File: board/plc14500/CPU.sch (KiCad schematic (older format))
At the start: 67 parts, among them U3 74HC14, U6 NE555, U7 74HC590A, U8 LH5168, U9 MC14500

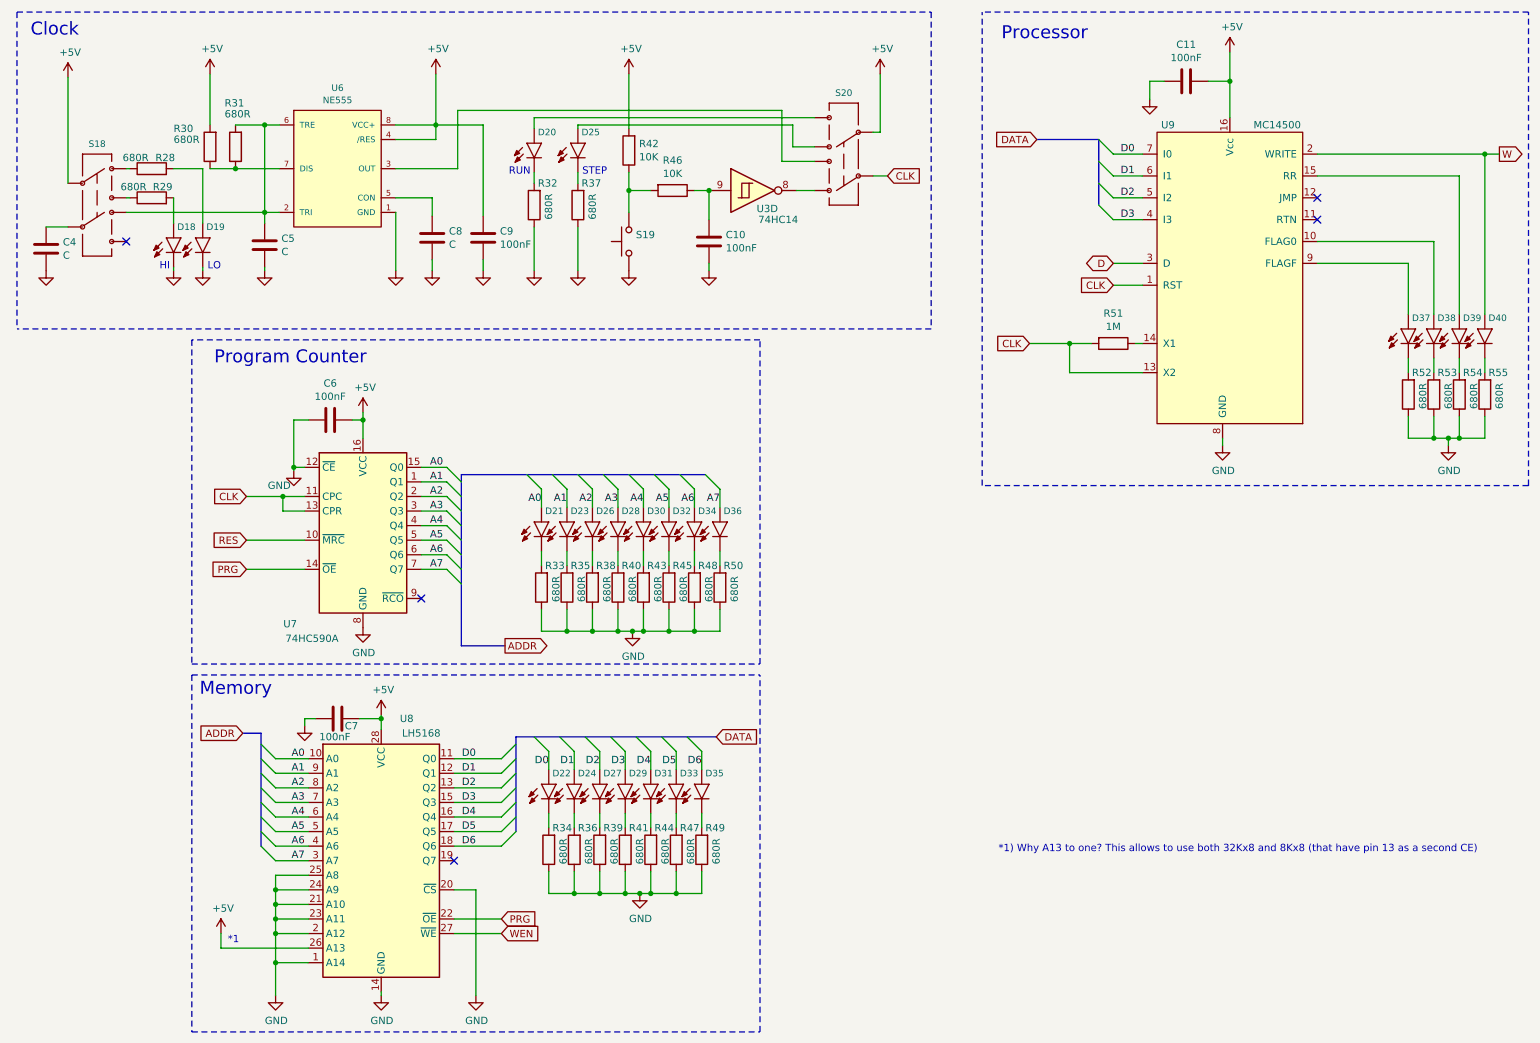
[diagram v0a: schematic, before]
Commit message: Schema updates, add loopback and timer
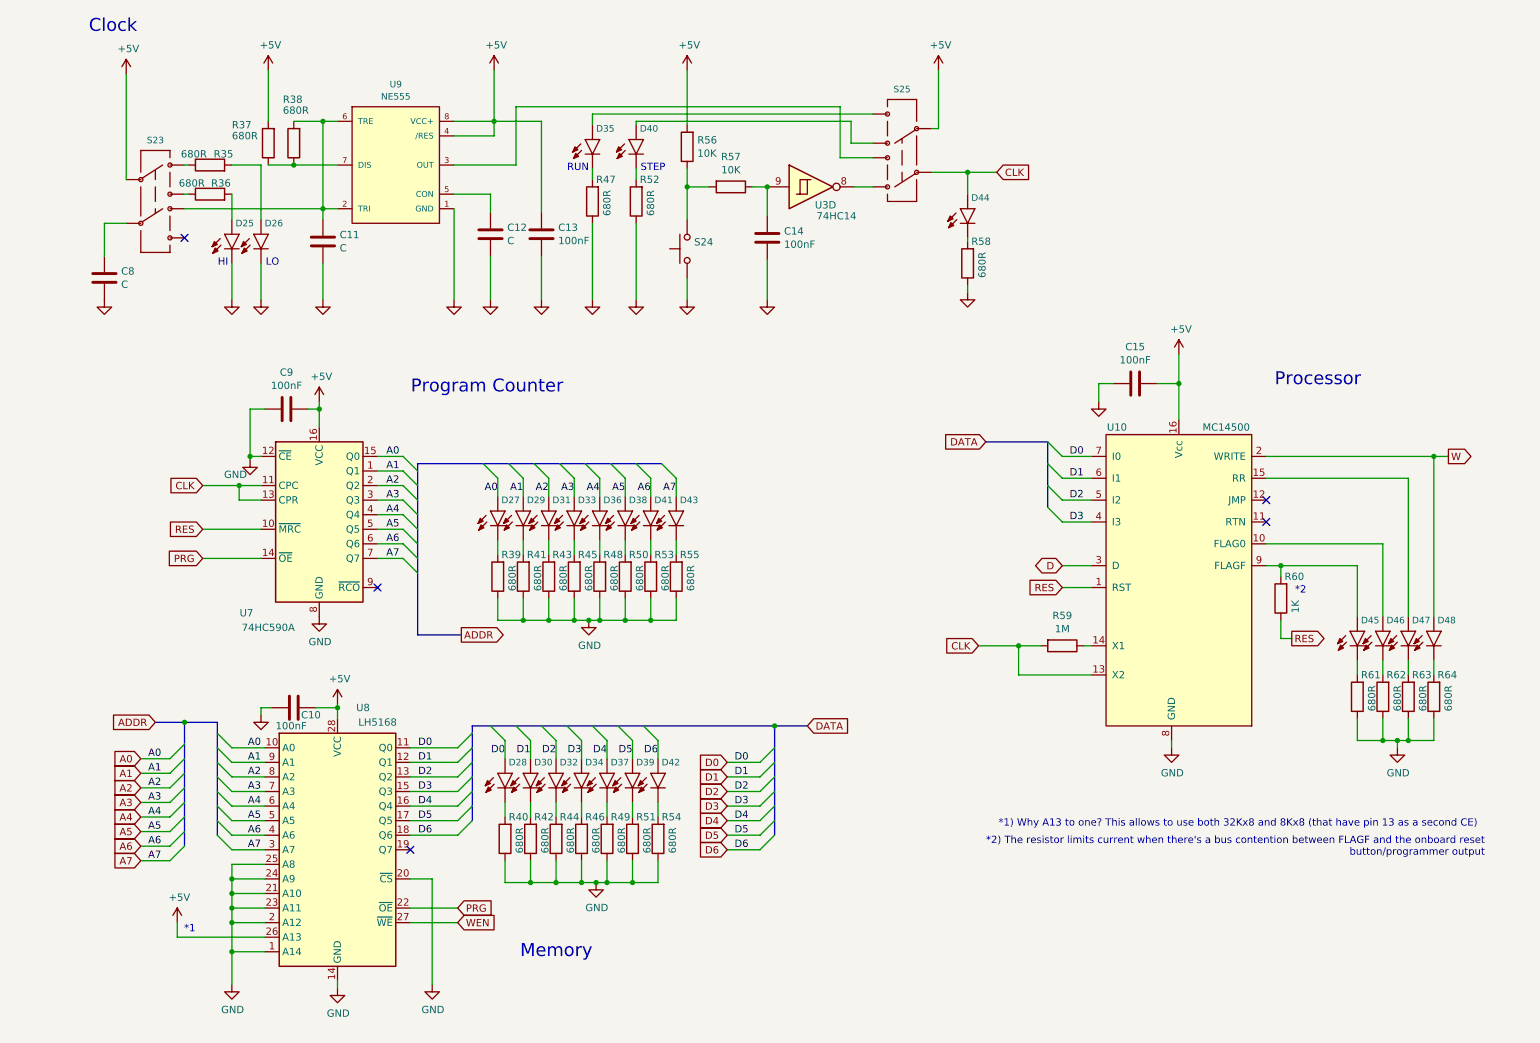
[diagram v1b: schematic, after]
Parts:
- added D44: LED5MM, plc14500:LED_5MM, symbol SparkFun-LED:LED5MM
- added R58: 680R, Resistor_THT:R_Axial_DIN0309_L9.0mm_D3.2mm_P12.70mm_Horizontal, symbol Device:R
- added R60: 1K, Resistor_THT:R_Axial_DIN0309_L9.0mm_D3.2mm_P12.70mm_Horizontal, symbol Device:R
- C10: renamed from C7; footprint (none) -> Capacitor_THT:C_Rect_L7.2mm_W2.5mm_P5.00mm_FKS2_FKP2_MKS2_MKP2
- C11: renamed from C5; footprint (none) -> Capacitor_THT:C_Rect_L7.2mm_W2.5mm_P5.00mm_FKS2_FKP2_MKS2_MKP2
- C12: renamed from C8; footprint (none) -> Capacitor_THT:C_Rect_L7.2mm_W2.5mm_P5.00mm_FKS2_FKP2_MKS2_MKP2
- C13: renamed from C9; footprint (none) -> Capacitor_THT:C_Rect_L7.2mm_W2.5mm_P5.00mm_FKS2_FKP2_MKS2_MKP2
- C14: renamed from C10; footprint (none) -> Capacitor_THT:C_Rect_L7.2mm_W2.5mm_P5.00mm_FKS2_FKP2_MKS2_MKP2
- C15: renamed from C11; footprint (none) -> Capacitor_THT:C_Rect_L7.2mm_W2.5mm_P5.00mm_FKS2_FKP2_MKS2_MKP2
- C8: renamed from C4; footprint (none) -> Capacitor_THT:C_Rect_L7.2mm_W2.5mm_P5.00mm_FKS2_FKP2_MKS2_MKP2
- C9: renamed from C6; footprint (none) -> Capacitor_THT:C_Rect_L7.2mm_W2.5mm_P5.00mm_FKS2_FKP2_MKS2_MKP2
- D25: renamed from D18; footprint LED_5MM -> plc14500:LED_5MM
- D26: renamed from D19; footprint LED_5MM -> plc14500:LED_5MM
- D27: renamed from D21; footprint LED_5MM -> plc14500:LED_5MM
- D28: renamed from D22; footprint LED_5MM -> plc14500:LED_5MM
- D29: renamed from D23; footprint LED_5MM -> plc14500:LED_5MM
- D30: renamed from D24; footprint LED_5MM -> plc14500:LED_5MM
- D31: renamed from D26; footprint LED_5MM -> plc14500:LED_5MM
- D32: renamed from D27; footprint LED_5MM -> plc14500:LED_5MM
- D33: renamed from D28; footprint LED_5MM -> plc14500:LED_5MM
- D34: renamed from D29; footprint LED_5MM -> plc14500:LED_5MM
- D35: renamed from D20; footprint LED_5MM -> plc14500:LED_5MM
- D36: renamed from D30; footprint LED_5MM -> plc14500:LED_5MM
- D37: renamed from D31; footprint LED_5MM -> plc14500:LED_5MM
- D38: renamed from D32; footprint LED_5MM -> plc14500:LED_5MM
- D39: renamed from D33; footprint LED_5MM -> plc14500:LED_5MM
- D40: renamed from D25; footprint LED_5MM -> plc14500:LED_5MM
- D41: renamed from D34; footprint LED_5MM -> plc14500:LED_5MM
- D42: renamed from D35; footprint LED_5MM -> plc14500:LED_5MM
- D43: renamed from D36; footprint LED_5MM -> plc14500:LED_5MM
- D45: renamed from D37; footprint LED_5MM -> plc14500:LED_5MM
- D46: renamed from D38; footprint LED_5MM -> plc14500:LED_5MM
- D47: renamed from D39; footprint LED_5MM -> plc14500:LED_5MM
- D48: renamed from D40; footprint LED_5MM -> plc14500:LED_5MM
- R35: renamed from R28; footprint (none) -> Resistor_THT:R_Axial_DIN0309_L9.0mm_D3.2mm_P12.70mm_Horizontal
- R36: renamed from R29; footprint (none) -> Resistor_THT:R_Axial_DIN0309_L9.0mm_D3.2mm_P12.70mm_Horizontal
- R37: renamed from R30; footprint (none) -> Resistor_THT:R_Axial_DIN0309_L9.0mm_D3.2mm_P12.70mm_Horizontal
- R38: renamed from R31; footprint (none) -> Resistor_THT:R_Axial_DIN0309_L9.0mm_D3.2mm_P12.70mm_Horizontal
- R39: renamed from R33; footprint (none) -> Resistor_THT:R_Axial_DIN0309_L9.0mm_D3.2mm_P12.70mm_Horizontal
- R40: renamed from R34; footprint (none) -> Resistor_THT:R_Axial_DIN0309_L9.0mm_D3.2mm_P12.70mm_Horizontal
- R41: renamed from R35; footprint (none) -> Resistor_THT:R_Axial_DIN0309_L9.0mm_D3.2mm_P12.70mm_Horizontal
- R42: renamed from R36; footprint (none) -> Resistor_THT:R_Axial_DIN0309_L9.0mm_D3.2mm_P12.70mm_Horizontal
- R43: renamed from R38; footprint (none) -> Resistor_THT:R_Axial_DIN0309_L9.0mm_D3.2mm_P12.70mm_Horizontal
- R44: renamed from R39; footprint (none) -> Resistor_THT:R_Axial_DIN0309_L9.0mm_D3.2mm_P12.70mm_Horizontal
- R45: renamed from R40; footprint (none) -> Resistor_THT:R_Axial_DIN0309_L9.0mm_D3.2mm_P12.70mm_Horizontal
- R46: renamed from R41; footprint (none) -> Resistor_THT:R_Axial_DIN0309_L9.0mm_D3.2mm_P12.70mm_Horizontal
- R47: renamed from R32; footprint (none) -> Resistor_THT:R_Axial_DIN0309_L9.0mm_D3.2mm_P12.70mm_Horizontal
- R48: renamed from R43; footprint (none) -> Resistor_THT:R_Axial_DIN0309_L9.0mm_D3.2mm_P12.70mm_Horizontal
- R49: renamed from R44; footprint (none) -> Resistor_THT:R_Axial_DIN0309_L9.0mm_D3.2mm_P12.70mm_Horizontal
- R50: renamed from R45; footprint (none) -> Resistor_THT:R_Axial_DIN0309_L9.0mm_D3.2mm_P12.70mm_Horizontal
- R51: renamed from R47; footprint (none) -> Resistor_THT:R_Axial_DIN0309_L9.0mm_D3.2mm_P12.70mm_Horizontal
- R52: renamed from R37; footprint (none) -> Resistor_THT:R_Axial_DIN0309_L9.0mm_D3.2mm_P12.70mm_Horizontal
- R53: renamed from R48; footprint (none) -> Resistor_THT:R_Axial_DIN0309_L9.0mm_D3.2mm_P12.70mm_Horizontal
- R54: renamed from R49; footprint (none) -> Resistor_THT:R_Axial_DIN0309_L9.0mm_D3.2mm_P12.70mm_Horizontal
- R55: renamed from R50; footprint (none) -> Resistor_THT:R_Axial_DIN0309_L9.0mm_D3.2mm_P12.70mm_Horizontal
- R56: renamed from R42; footprint (none) -> Resistor_THT:R_Axial_DIN0309_L9.0mm_D3.2mm_P12.70mm_Horizontal
- R57: renamed from R46; footprint (none) -> Resistor_THT:R_Axial_DIN0309_L9.0mm_D3.2mm_P12.70mm_Horizontal
- R59: renamed from R51; footprint (none) -> Resistor_THT:R_Axial_DIN0309_L9.0mm_D3.2mm_P12.70mm_Horizontal
- R61: renamed from R52; footprint (none) -> Resistor_THT:R_Axial_DIN0309_L9.0mm_D3.2mm_P12.70mm_Horizontal
- R62: renamed from R53; footprint (none) -> Resistor_THT:R_Axial_DIN0309_L9.0mm_D3.2mm_P12.70mm_Horizontal
- R63: renamed from R54; footprint (none) -> Resistor_THT:R_Axial_DIN0309_L9.0mm_D3.2mm_P12.70mm_Horizontal
- R64: renamed from R55; footprint (none) -> Resistor_THT:R_Axial_DIN0309_L9.0mm_D3.2mm_P12.70mm_Horizontal
- S23: renamed from S18; footprint SWITCH_DPDT_PTH_GPI-152-3013 -> plc14500:SWITCH_DPDT
- S24: renamed from S19; footprint (none) -> Button_Switch_THT:SW_Tactile_Straight_KSA0Axx1LFTR
- S25: renamed from S20; footprint SWITCH_DPDT_PTH_GPI-152-3013 -> plc14500:SWITCH_DPDT
- U10: renamed from U9; footprint (none) -> Package_DIP:DIP-16_W7.62mm_LongPads
- U7: footprint (none) -> Package_DIP:DIP-16_W7.62mm_LongPads
- renumbered U6 to U9
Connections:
- net CLK: now also D44.A; no longer U10.1 (RST)
- net GND: now also R58.1
- net RES: now also U10.1 (RST), R60.1
- net at D45.A, U10.9 (FLAGF): now also R60.2
- new net: D44.K (C), R58.2
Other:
- note added: "*2"
- note added: "*2) The resistor limits current when there's a bus contention between FLAGF and the onboard reset\nbutton/programmer output"
- moved on the sheet: C10, C11, C12, C13, C14, C15, C8, C9, D25, D26, D27, D28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

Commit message: Add scratchpad ram
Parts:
- renumbered U7 to U10, U8 to U11, U9 to U12, U10 to U13
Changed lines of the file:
@@
 $Descr A4 11693 8268
 encoding utf-8
-Sheet 3 3
+Sheet 3 4
 Title "PLC14500 - Nano"
 Date "2022-11-07"
@@
 P 3325 1750
 AR Path="/63980606" Ref="U?"  Part="1"
-AR Path="/6394A5B3/63980606" Ref="U9"  Part="1"
-F 0 "U9" H 3325 2304 45  0000 C CNN
+AR Path="/6394A5B3/63980606" Ref="U12"  Part="1"
+F 0 "U12" H 3325 2304 45  0000 C CNN
 F 1 "NE555" H 3325 2220 45  0000 C CNN
 F 2 "Package_DIP:DIP-8_W7.62mm" H 3325 2250 20  0001 C CNN
@@
 P 2800 4250
 AR Path="/6398063A" Ref="U?"  Part="1"
-AR Path="/6394A5B3/6398063A" Ref="U7"  Part="1"
-F 0 "U7" H 2300 3675 50  0000 C CNN
+AR Path="/6394A5B3/6398063A" Ref="U10"  Part="1"
+F 0 "U10" H 2300 3675 50  0000 C CNN
 F 1 "74HC590A" H 2450 3575 50  0000 C CNN
 F 2 "Package_DIP:DIP-16_W7.62mm_LongPads" H 2800 4300 50  0001 C CNN
@@
 P 2925 6450
 AR Path="/63980925" Ref="U?"  Part="1"
-AR Path="/6394A5B3/63980925" Ref="U8"  Part="1"
-F 0 "U8" H 3100 7425 50  0000 C CNN
+AR Path="/6394A5B3/63980925" Ref="U11"  Part="1"
+F 0 "U11" H 3100 7425 50  0000 C CNN
 F 1 "LH5168" H 3200 7325 50  0000 C CNN
 F 2 "Package_DIP:DIP-28_W15.24mm" H 2925 6350 50  0001 C CNN
@@
 P 8500 3450
 AR Path="/63980933" Ref="U?"  Part="1"
-AR Path="/6394A5B3/63980933" Ref="U10"  Part="1"
-F 0 "U10" H 8275 3350 50  0000 C CNN
+AR Path="/6394A5B3/63980933" Ref="U13"  Part="1"
+F 0 "U13" H 8275 3350 50  0000 C CNN
 F 1 "MC14500" H 9025 3350 50  0000 C CNN
 F 2 "Package_DIP:DIP-16_W7.62mm_LongPads" H 8500 3450 50  0001 C CNN

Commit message: Schematic tweaks
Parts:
- removed C8: C, Capacitor_THT:C_Rect_L7.2mm_W2.5mm_P5.00mm_FKS2_FKP2_MKS2_MKP2, symbol Device:C
- added C7: 10uF, Capacitor_THT:CP_Radial_D8.0mm_P5.00mm, symbol SparkFun-Capacitors:1000UF-RADIAL-5MM-25V-20%
- added D37: LED 5MM Red, plc14500:LED_5MM, symbol SparkFun-LED:LED5MM
- added R49: 680R, Resistor_THT:R_Axial_DIN0309_L9.0mm_D3.2mm_P12.70mm_Horizontal, symbol Device:R
- C10: renamed from C11; value C -> 100nF; Price (none) -> 0.02
- C11: renamed from C12; value C -> 100nF; Price (none) -> 0.02
- C12: renamed from C13; Price (none) -> 0.02
- C13: renamed from C14; Price (none) -> 0.02
- C14: renamed from C15; Price (none) -> 0.02
- C8: renamed from C9; Price (none) -> 0.02
- C9: renamed from C10; Price (none) -> 0.02
- D18: renamed from D25; value LED5MM -> LED 5MM Red; Price (none) -> 0.01
- D19: renamed from D26; value LED5MM -> LED 5MM Red; Price (none) -> 0.01
- D20: renamed from D27; value LED5MM -> LED 5MM Red; Price (none) -> 0.01
- D21: renamed from D28; value LED5MM -> LED 5MM Red; Price (none) -> 0.01
- D22: renamed from D29; value LED5MM -> LED 5MM Red; Price (none) -> 0.01
- D23: renamed from D30; value LED5MM -> LED 5MM Red; Price (none) -> 0.01
- D24: renamed from D31; value LED5MM -> LED 5MM Red; Price (none) -> 0.01
- D25: renamed from D32; value LED5MM -> LED 5MM Red; Price (none) -> 0.01
- D26: renamed from D33; value LED5MM -> LED 5MM Red; Price (none) -> 0.01
- D27: renamed from D34; value LED5MM -> LED 5MM Red; Price (none) -> 0.01
- D28: renamed from D35; value LED5MM -> LED 5MM Red; Price (none) -> 0.01
- D29: renamed from D36; value LED5MM -> LED 5MM Red; Price (none) -> 0.01
- D30: renamed from D37; value LED5MM -> LED 5MM Red; Price (none) -> 0.01
- D31: renamed from D38; value LED5MM -> LED 5MM Red; Price (none) -> 0.01
- D32: renamed from D39; value LED5MM -> LED 5MM Red; Price (none) -> 0.01
- D33: renamed from D40; value LED5MM -> LED 5MM Red; Price (none) -> 0.01
- D34: renamed from D41; value LED5MM -> LED 5MM Red; Price (none) -> 0.01
- D35: renamed from D42; value LED5MM -> LED 5MM Red; Price (none) -> 0.01
- D36: renamed from D43; value LED5MM -> LED 5MM Red; Price (none) -> 0.01
- D38: renamed from D44; value LED5MM -> LED 5MM Red; Price (none) -> 0.01
- D39: renamed from D45; value LED5MM -> LED 5MM Red; Price (none) -> 0.01
- D40: renamed from D46; value LED5MM -> LED 5MM Red; Price (none) -> 0.01
- D41: renamed from D47; value LED5MM -> LED 5MM Red; Price (none) -> 0.01
- D42: renamed from D48; value LED5MM -> LED 5MM Red; Price (none) -> 0.01
- R28: renamed from R35; Price (none) -> 0.01
- R29: renamed from R36; Price (none) -> 0.01
- R30: renamed from R37; Price (none) -> 0.01
- R31: renamed from R38; Price (none) -> 0.01
- R32: renamed from R39; Price (none) -> 0.01
- R33: renamed from R40; Price (none) -> 0.01
- R34: renamed from R41; Price (none) -> 0.01
- R35: renamed from R42; Price (none) -> 0.01
- R36: renamed from R43; Price (none) -> 0.01
- R37: renamed from R44; Price (none) -> 0.01
- R38: renamed from R45; Price (none) -> 0.01
- R39: renamed from R46; Price (none) -> 0.01
- R40: renamed from R47; Price (none) -> 0.01
- R41: renamed from R48; Price (none) -> 0.01
- R42: renamed from R49; Price (none) -> 0.01
- R43: renamed from R50; Price (none) -> 0.01
- R44: renamed from R51; Price (none) -> 0.01
- R45: renamed from R52; Price (none) -> 0.01
- R46: renamed from R53; Price (none) -> 0.01
- R47: renamed from R54; Price (none) -> 0.01
- R48: renamed from R55; Price (none) -> 0.01
- R50: renamed from R56; Price (none) -> 0.01
- R51: renamed from R57; Price (none) -> 0.01
- R52: renamed from R58; Price (none) -> 0.01
- R53: renamed from R59; Price (none) -> 0.01
- R54: renamed from R60; Price (none) -> 0.01
- R55: renamed from R61; Price (none) -> 0.01
- R56: renamed from R62; Price (none) -> 0.01
- R57: renamed from R63; Price (none) -> 0.01
- R58: renamed from R64; Price (none) -> 0.01
- S16: renamed from S23; value SWITCH-DPDT-PTH-GPI-152-3013 -> Switch DPDT; Price (none) -> 0.69
- S17: renamed from S24; value SW_Push -> Push Button; Price (none) -> 0.01
- S18: renamed from S25; value SWITCH-DPDT-PTH-GPI-152-3013 -> Switch DPDT; Price (none) -> 0.69
- U10: renamed from U13; Price (none) -> 2.6
- U3: footprint (none) -> Package_DIP:DIP-14_W7.62mm_LongPads; Price (none) -> 0.16
- U7: renamed from U10; Price (none) -> 0.43
- U8: renamed from U11; Price (none) -> 1.2
- U9: renamed from U12; Price (none) -> 0.07
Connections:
- net GND: now also C7.-, R49.1
- net at S16.6: now also C7.+
- net D7: now reaches U8.19 (Q7)
- net D7: now also D37.A
- new net: D37.K (C), R49.2
- no-connect marks 5 -> 4
